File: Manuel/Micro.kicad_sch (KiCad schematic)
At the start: 3 parts, among them U6 ESP32-DEVKITC

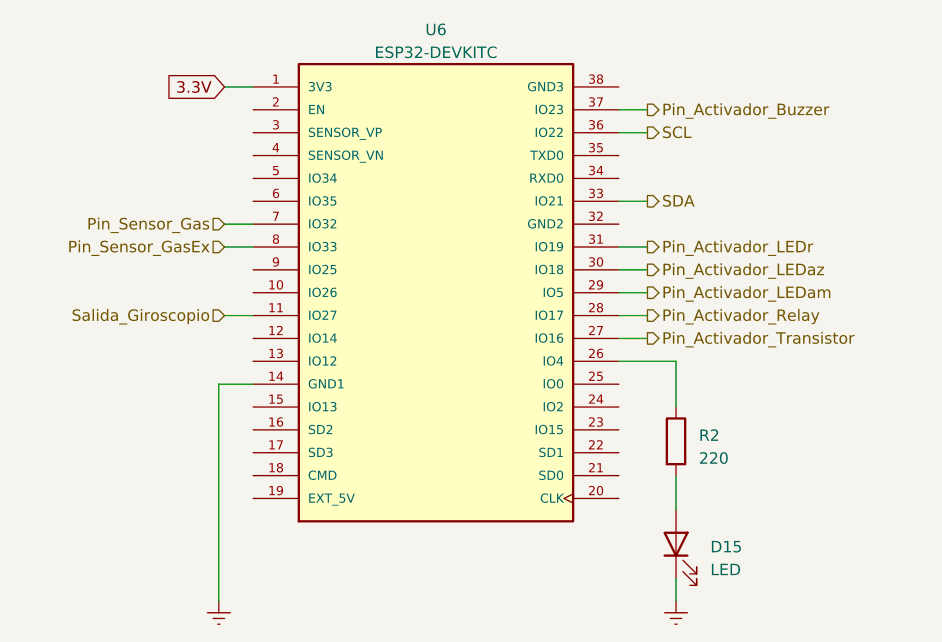
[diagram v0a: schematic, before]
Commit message: Proyecto Kiss V2
Esquemático y PCB terminados
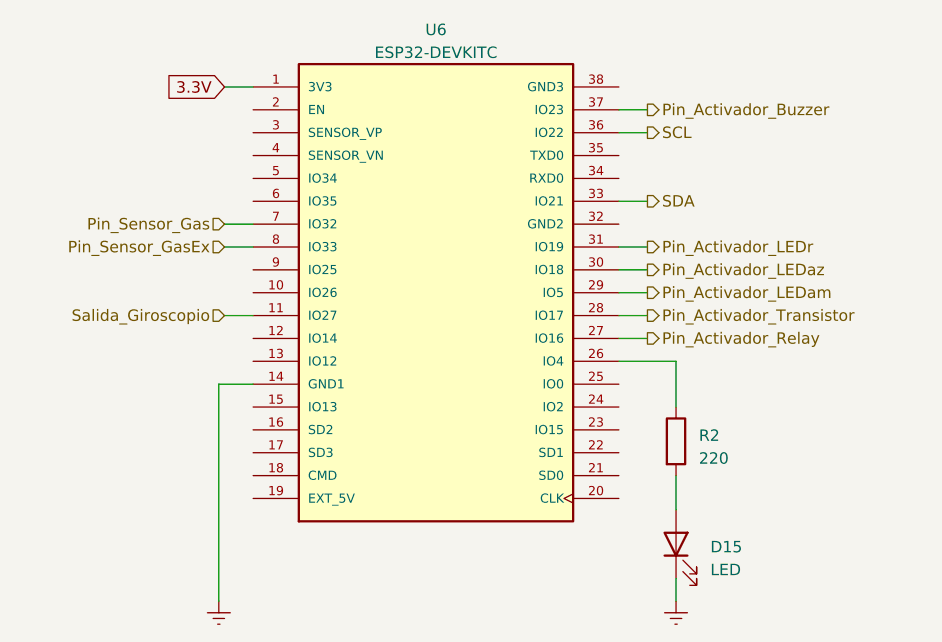
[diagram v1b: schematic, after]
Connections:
- net Pin_Activador_Relay: now also U6.27 (IO16); no longer U6.28 (IO17)
- net Pin_Activador_Transistor: now also U6.28 (IO17); no longer U6.27 (IO16)
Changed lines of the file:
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@@
 (kicad_sch (version 20230121) (generator eeschema)
   (paper "A4")
+  (wire (pts (xy 167.005 103.505) (xy 170.18 103.505))
+    (stroke (width 0) (type default))
+  )
   (wire (pts (xy 167.005 95.885) (xy 170.18 95.885))
     (stroke (width 0) (type default))
@@
   )
   (wire (pts (xy 167.005 88.265) (xy 170.18 88.265))
-    (stroke (width 0) (type default))
-  )
-  (wire (pts (xy 167.005 103.505) (xy 170.18 103.505))
     (stroke (width 0) (type default))
   )
@@
     (effects (font (size 1.27 1.27)) (justify left))
   )
-  (hierarchical_label "Pin_Activador_Relay" (shape output) (at 170.18 100.965 0) (fields_autoplaced)
+  (hierarchical_label "Pin_Activador_Relay" (shape output) (at 170.18 103.505 0) (fields_autoplaced)
     (effects (font (size 1.27 1.27)) (justify left))
   )
@@
     (effects (font (size 1.27 1.27)) (justify right))
   )
-  (hierarchical_label "Pin_Activador_Transistor" (shape output) (at 170.18 103.505 0) (fields_autoplaced)
+  (hierarchical_label "Pin_Activador_Transistor" (shape output) (at 170.18 100.965 0) (fields_autoplaced)
     (effects (font (size 1.27 1.27)) (justify left))
   )
